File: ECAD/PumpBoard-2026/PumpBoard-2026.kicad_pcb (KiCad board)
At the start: 2 copper layers, 30 x 28 mm, 18 parts, among them J1 Conn_01x04, J3 CON_EV, J4 CON_PUMP, Q1 AO3400A, Q2 AO3400A

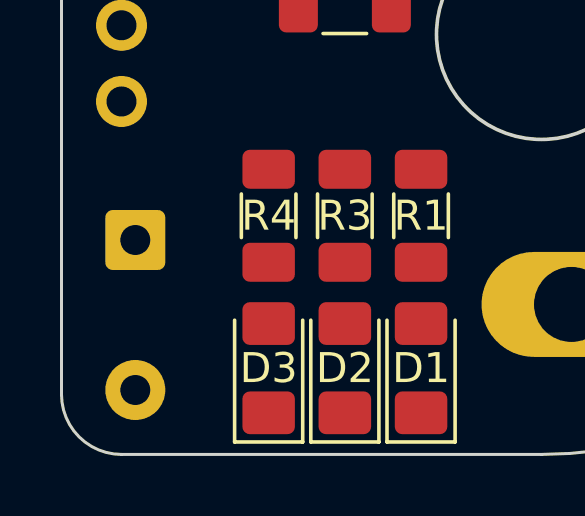
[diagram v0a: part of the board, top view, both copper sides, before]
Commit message: change capacitor size
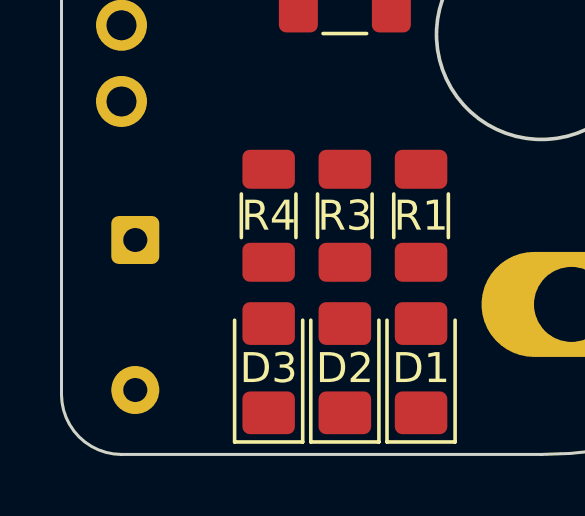
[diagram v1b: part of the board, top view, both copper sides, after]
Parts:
- C2: footprint Capacitor_THT:CP_Radial_D10.0mm_P5.00mm -> Capacitor_THT:CP_Radial_D8.0mm_P5.00mm
